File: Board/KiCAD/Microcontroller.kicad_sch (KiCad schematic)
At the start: 28 parts, among them J2 Conn_ARM_SWD_TagConnect_TC2030, J4 Conn_01x03, SW2 SW_Push, U5 LMR50410, U9 STM32F103C8T6, Y1 Crystal_GND24_Small, Y4 CM8V-T1A-32.768KHZ-12.5PF-20P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

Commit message: Team #6 - Battery Management Module Rev 1 - PCB
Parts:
- added TP39: TestPoint_Small, TestPoint:TestPoint_THTPad_1.0x1.0mm_Drill0.5mm, symbol Connector:TestPoint_Small
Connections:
- net 3.3V: now also TP39.1
- net CHRG_OK: now reaches U9.11 (PA1)
- no-connect marks 17 -> 16

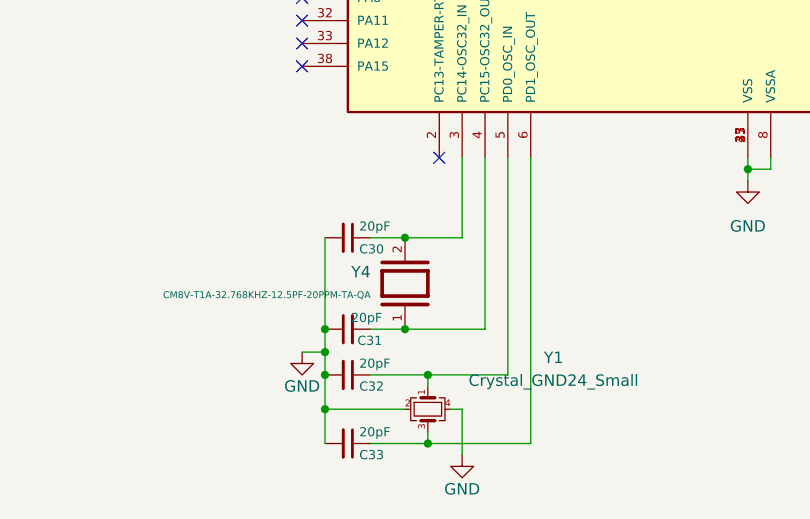
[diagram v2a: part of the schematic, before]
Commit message: Fixed Library paths for component symbol
@andrewgreenberg @KeytarGoblin
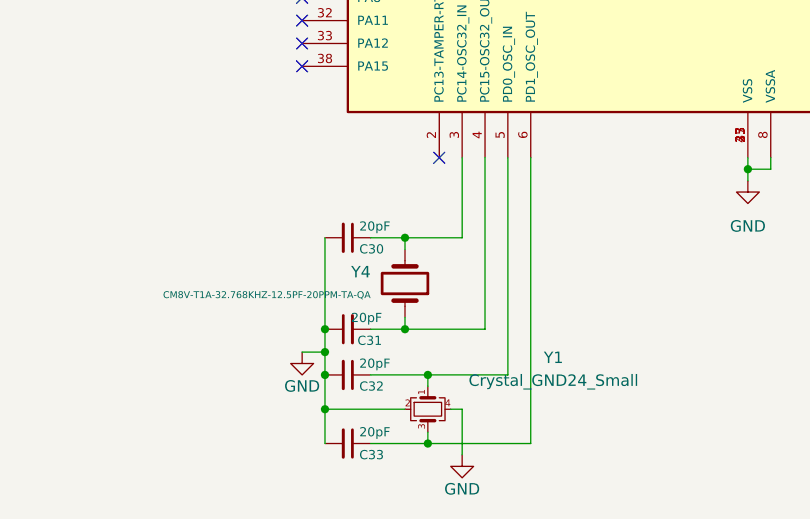
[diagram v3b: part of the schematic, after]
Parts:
- Y4: symbol CM8V-T1A-32.768KHZ-12.5PF-20PPM-TA-QA:CM8V-T1A-32.768KHZ-12.5PF-20PPM-TA-QA -> Device:Crystal
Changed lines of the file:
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@@
 	)
 	(junction
-		(at 102.87 166.37)
-		(diameter 0)
-		(color 0 0 0 0)
-	)
-	(junction
 		(at 193.04 91.44)
 		(diameter 0)
@@
 	)
 	(junction
+		(at 102.87 166.37)
+		(diameter 0)
+		(color 0 0 0 0)
+	)
+	(junction
 		(at 196.85 104.14)
 		(diameter 0)
@@
 	(wire
 		(pts
+			(xy 102.87 157.48) (xy 102.87 156.21)
+		)
+		(stroke
+			(width 0)
+			(type default)
+		)
+	)
+	(wire
+		(pts
 			(xy 105.41 177.8) (xy 105.41 179.07)
 		)
@@
 	(wire
 		(pts
+			(xy 102.87 165.1) (xy 102.87 166.37)
+		)
+		(stroke
+			(width 0)
+			(type default)
+		)
+	)
+	(wire
+		(pts
 			(xy 97.79 55.88) (xy 107.95 55.88)
 		)
@@
 	(wire
 		(pts
+			(xy 102.87 166.37) (xy 111.76 166.37)
+		)
+		(stroke
+			(width 0)
+			(type default)
+		)
+	)
+	(wire
+		(pts
 			(xy 154.94 44.45) (xy 157.48 44.45)
 		)
@@
 	(wire
 		(pts
-			(xy 102.87 156.21) (xy 109.22 156.21)
-		)
-		(stroke
-			(width 0)
-			(type default)
-		)
-	)
-	(wire
-		(pts
 			(xy 193.04 97.79) (xy 193.04 101.6)
 		)
@@
 	(wire
 		(pts
-			(xy 102.87 166.37) (xy 111.76 166.37)
+			(xy 90.17 92.71) (xy 91.44 92.71)
 		)
 		(stroke
@@
 	(wire
 		(pts
-			(xy 90.17 92.71) (xy 91.44 92.71)
+			(xy 128.27 58.42) (xy 130.81 58.42)
 		)
 		(stroke
@@
 	(wire
 		(pts
-			(xy 128.27 58.42) (xy 130.81 58.42)
+			(xy 118.11 48.26) (xy 118.11 50.8)
 		)
 		(stroke
@@
 	(wire
 		(pts
-			(xy 118.11 48.26) (xy 118.11 50.8)
+			(xy 83.82 127) (xy 91.44 127)
 		)
 		(stroke
@@
 	(wire
 		(pts
-			(xy 83.82 127) (xy 91.44 127)
+			(xy 200.66 91.44) (xy 200.66 92.71)
 		)
 		(stroke
@@
 	(wire
 		(pts
-			(xy 200.66 91.44) (xy 200.66 92.71)
+			(xy 55.88 45.72) (xy 68.58 45.72)
 		)
 		(stroke
@@
 	(wire
 		(pts
-			(xy 55.88 45.72) (xy 68.58 45.72)
+			(xy 139.7 39.37) (xy 157.48 39.37)
 		)
 		(stroke
@@
 	(wire
 		(pts
-			(xy 139.7 39.37) (xy 157.48 39.37)
+			(xy 102.87 156.21) (xy 109.22 156.21)
 		)
 		(stroke
@@
 	)
 	(symbol
-		(lib_id "CM8V-T1A-32.768KHZ-12.5PF-20PPM-TA-QA:CM8V-T1A-32.768KHZ-12.5PF-20PPM-TA-QA")
+		(lib_id "Device:Crystal")
 		(at 102.87 161.29 270)
 		(mirror x)

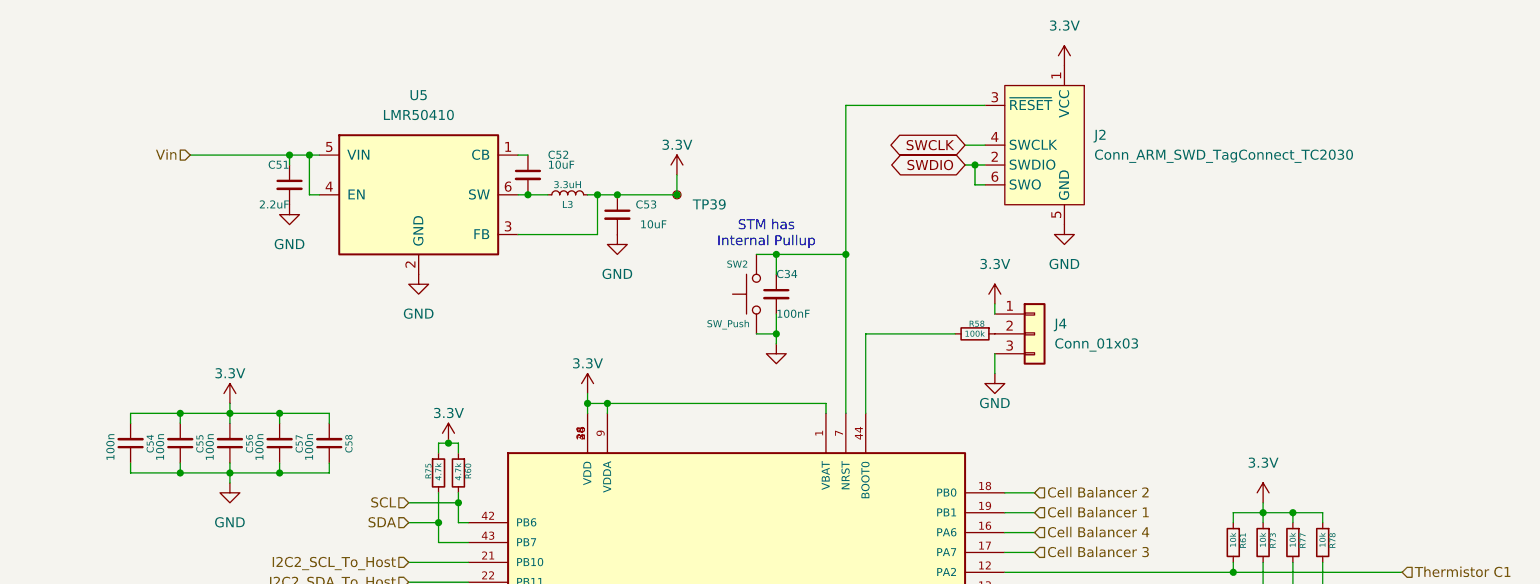
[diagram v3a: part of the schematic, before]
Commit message: Polish on schematic and board. Changed balance resistors to 100 ohms. Lots of silly OCD cleanup and documentation. Board has thicker (0.2mm) I2C lines, cleaned up 3.3V connections to reduce impedance, lots of other small tweaks.
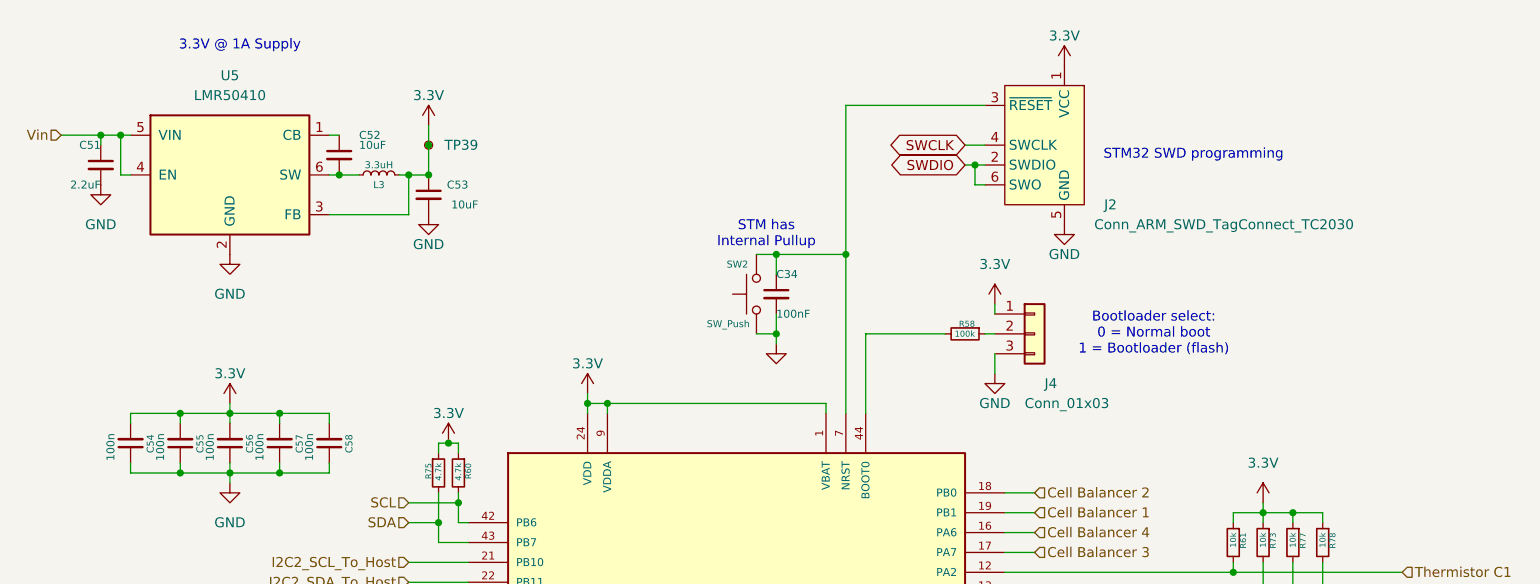
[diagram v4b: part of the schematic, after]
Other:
- note added: "3.3V @ 1A Supply"
- note added: "Bootloader select: 0 = Normal boot 1 = Bootloader (flash)"
- note added: "STM32 SWD programming"
- moved on the sheet: C51, C52, C53, L3, R58, TP39, U5

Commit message: Started updating BOM with MFR/MPN
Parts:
- C30, C31, C32, C33: value 20pF -> 20p
- C34: value 100nF -> 100n
- C51: value 2.2uF -> 2.2u
- C52, C53: value 10uF -> 10u
- L3: value 3.3uH -> 3.3u
- R60, R75: MPN (none) -> RMCF0603FT4K70
- R61, R73, R77, R78: MFR (none) -> Stackpole Electronics Inc; MPN (none) -> RMCF0603FT10K0
- Y4: Availability In Stock -> (none); Check_prices https://www.snapeda.com/parts/CM8V-T1A-32.768KHZ-12.5PF-20P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 -> (none); Description_1 32.768 kHz ±20ppm Crystal 12.5pF 70 kOhms 2-SMD, No Lead -> (none); MANUFACTURER Micro Crystal -> (none); MAXIMUM_PACKAGE_HEIGHT 0.6 mm -> (none); PARTREV 1.3/03.2021 -> (none); Package SMD-2 Micro Crystal -> (none); Price None -> (none); STANDARD Manufacturer Recommendations -> (none); SnapEDA_Link https://www.snapeda.com/parts/CM8V-T1A-32.768KHZ-12.5PF-20P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 -> (none)

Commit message: BOM Complete Need a Once Over Check
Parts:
- C30, C31, C32, C33: MFR (none) -> Aillen; MPN (none) -> 3372-0603N200J251SDTR-ND; Package (none) -> 0603N200J251SD
- C34, C54, C55, C56, C57, C58: MFR (none) -> Aillen; MPN (none) -> 3372-0603B104K500XDTR-ND; Package (none) -> 0603B104K500XD
- C51: MFR (none) -> Aillen; MPN (none) -> 3372-1206B104K500BDTR-ND; Package (none) -> 1206B104K500BD
- C52, C53: MFR SAMSUNG -> Samsung Electro-Mechanics; MPN CL31A106KBHNNNE -> 1276-1804-1-ND; Package (none) -> CL31B106KAHNNNE
- J2: MFR (none) -> Tag-Connect LLC; MPN (none) -> TC2030-CTX-ND; Package (none) -> TC2030-CTX
- J4: MFR (none) -> Würth Elektronik; MPN (none) -> 732-5316-ND; Package (none) -> 61300311121
- L3: MFR (none) -> Taiyo Yuden; MPN (none) -> 587-3227-1-ND; Package (none) -> MAMK2520T3R3M
- R58: MFR (none) -> Stackpole Electronics Inc; MPN (none) -> RMCF0603FT100KCT-ND; Package (none) -> RMCF0603FT100K
- R60, R75: MFR (none) -> Stackpole Electronics Inc; MPN RMCF0603FT4K70 -> RMCF0603FT4K70CT-ND; Package (none) -> RMCF0603FT4K70
- R61, R73, R77, R78: MPN RMCF0603FT10K0 -> RMCF0603FT10K0CT-ND; Package (none) -> RMCF0603FT10K0
- SW2: MFR (none) -> C&K; MPN (none) -> CKN12220-1-ND; Package (none) -> PTS526SM15SMTR2 LFS
- U5: MFR (none) -> Texas Instruments; MPN (none) -> 296-LMR50410XFDBVRCT-ND; Package (none) -> LMR50410XFDBVR
- U9: Package (none) -> STM32F103C8T6
- Y1: Package (none) -> 7V-8.000MDDQ-T
- Y4: Package (none) -> CM8V-T1A-32.768KHZ-12.5PF-20PPM-TA-QA

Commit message: Updated schematic
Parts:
- R58: Package RMCF0603FT100K -> MCF0603FT100K
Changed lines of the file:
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@@
 					(size 1.27 1.27)
 				)
+				(hide yes)
 			)
 		)
@@
 					(size 1.27 1.27)
 				)
+				(hide yes)
 			)
 		)
@@
 					(size 1.27 1.27)
 				)
+				(hide yes)
 			)
 		)
@@
 					(size 1.27 1.27)
 				)
+				(hide yes)
 			)
 		)
@@
 					(size 1.27 1.27)
 				)
+				(hide yes)
 			)
 		)
@@
 					(size 1.27 1.27)
 				)
+				(hide yes)
 			)
 		)
@@
 					(size 1.27 1.27)
 				)
+				(hide yes)
 			)
 		)
@@
 					(size 1.27 1.27)
 				)
+				(hide yes)
 			)
 		)
@@
 					(size 1.27 1.27)
 				)
+				(hide yes)
 			)
 		)
@@
 					(size 1.27 1.27)
 				)
+				(hide yes)
 			)
 		)
@@
 					(size 1.27 1.27)
 				)
+				(hide yes)
 			)
 		)
@@
 					(size 1.27 1.27)
 				)
+				(hide yes)
 			)
 		)
@@
 					(size 1.27 1.27)
 				)
+				(hide yes)
 			)
 		)
@@
 					(size 1.27 1.27)
 				)
+				(hide yes)
 			)
 		)
@@
 					(size 1.27 1.27)
 				)
+				(hide yes)
 			)
 		)
@@
 					(size 1.27 1.27)
 				)
+				(hide yes)
 			)
 		)
@@
 					(size 1.27 1.27)
 				)
+				(hide yes)
 			)
 		)
@@
 					(size 1.27 1.27)
 				)
+				(hide yes)
 			)
 		)
@@
 					(size 1.27 1.27)
 				)
+				(hide yes)
 			)
 		)
@@
 					(size 1.27 1.27)
 				)
+				(hide yes)
 			)
 		)
@@
 					(size 1.27 1.27)
 				)
+				(hide yes)
 			)
 		)
@@
 			)
 		)
-		(property "Package" "RMCF0603FT100K"
+		(property "Package" "MCF0603FT100K"
 			(at 154.94 68.58 0)
 			(effects
@@
 					(size 1.27 1.27)
 				)
+				(hide yes)
 			)
 		)
@@
 					(size 1.27 1.27)
 				)
+				(hide yes)
 			)
 		)
@@
 					(size 1.27 1.27)
 				)
+				(hide yes)
 			)
 		)
@@
 					(size 1.27 1.27)
 				)
+				(hide yes)
 			)
 		)
@@
 					(size 1.27 1.27)
 				)
+				(hide yes)
 			)
 		)
@@
 					(size 1.27 1.27)
 				)
+				(hide yes)
 			)
 		)
@@
 					(size 1.27 1.27)
 				)
+				(hide yes)
 			)
 		)
@@
 					(size 1.27 1.27)
 				)
+				(hide yes)
 			)
 		)
@@
 					(size 1.27 1.27)
 				)
+				(hide yes)
 			)
 		)
@@
 					(size 1.27 1.27)
 				)
+				(hide yes)
 			)
 		)
@@
 					(size 1.27 1.27)
 				)
+				(hide yes)
 			)
 		)
@@
 					(size 1.27 1.27)
 				)
+				(hide yes)
 			)
 		)
@@
 					(size 1.27 1.27)
 				)
+				(hide yes)
 			)
 		)
@@
 					(size 1.27 1.27)
 				)
+				(hide yes)
 			)
 		)
@@
 					(size 1.27 1.27)
 				)
+				(hide yes)
 			)
 		)
@@
 					(size 1.27 1.27)
 				)
+				(hide yes)
 			)
 		)
@@
 					(size 1.27 1.27)
 				)
+				(hide yes)
 			)
 		)
@@
 					(size 1.27 1.27)
 				)
+				(hide yes)
 			)
 		)
@@
 					(size 1.27 1.27)
 				)
+				(hide yes)
 			)
 		)
@@
 					(size 1.27 1.27)
 				)
+				(hide yes)
 			)
 		)
@@
 					(size 1.27 1.27)
 				)
+				(hide yes)
 			)
 		)
@@
 					(size 1.27 1.27)
 				)
+				(hide yes)
 			)
 		)
@@
 					(size 1.27 1.27)
 				)
+				(hide yes)
 			)
 		)
@@
 					(size 1.27 1.27)
 				)
+				(hide yes)
 			)
 		)
@@
 					(size 1.27 1.27)
 				)
+				(hide yes)
 			)
 		)
@@
 					(size 1.27 1.27)
 				)
+				(hide yes)
 			)
 		)
@@
 					(size 1.27 1.27)
 				)
+				(hide yes)
 			)
 		)
@@
 					(size 1.27 1.27)
 				)
+				(hide yes)
 			)
 		)
@@
 					(size 1.27 1.27)
 				)
+				(hide yes)
 			)
 		)
@@
 					(size 1.27 1.27)
 				)
+				(hide yes)
 			)
 		)
@@
 					(size 1.27 1.27)
 				)
+				(hide yes)
 			)
 		)
@@
 					(size 1.27 1.27)
 				)
+				(hide yes)
 			)
 		)
@@
 					(size 1.27 1.27)
 				)
+				(hide yes)
 			)
 		)
@@
 					(size 1.27 1.27)
 				)
+				(hide yes)
 			)
 		)
@@
 					(size 1.27 1.27)
 				)
+				(hide yes)
 			)
 		)
@@
 					(size 1.27 1.27)
 				)
+				(hide yes)
 			)
 		)
@@
 					(size 1.27 1.27)
 				)
+				(hide yes)
 			)
 		)
@@
 					(size 1.27 1.27)
 				)
+				(hide yes)
 			)
 		)
@@
 					(size 1.27 1.27)
 				)
+				(hide yes)
 			)
 		)
@@
 					(size 1.27 1.27)
 				)
+				(hide yes)
 			)
 		)
@@
 					(size 1.27 1.27)
 				)
+				(hide yes)
 			)
 		)
@@
 					(size 1.27 1.27)
 				)
+				(hide yes)
 			)
 		)
